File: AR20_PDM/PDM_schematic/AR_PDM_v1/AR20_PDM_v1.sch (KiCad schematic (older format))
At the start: 9 parts, among them J1 High_Curret_terminal, J2 ACM_Connector

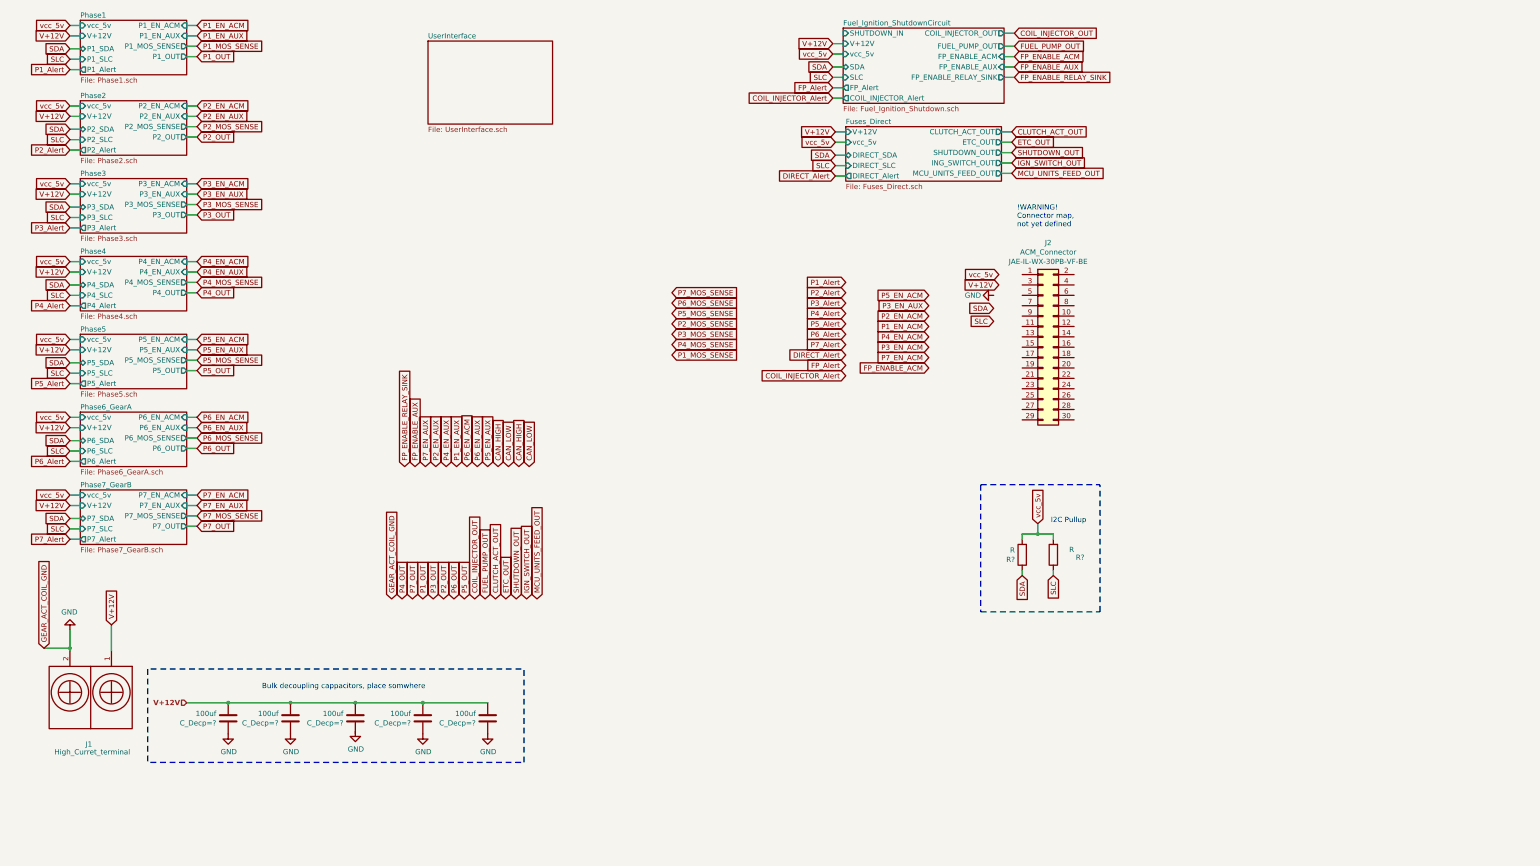
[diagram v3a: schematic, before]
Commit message: Added LEDs and switches.
- Added all status leds
- Added all switches
- ! Connections are work in progress, not everything is correct
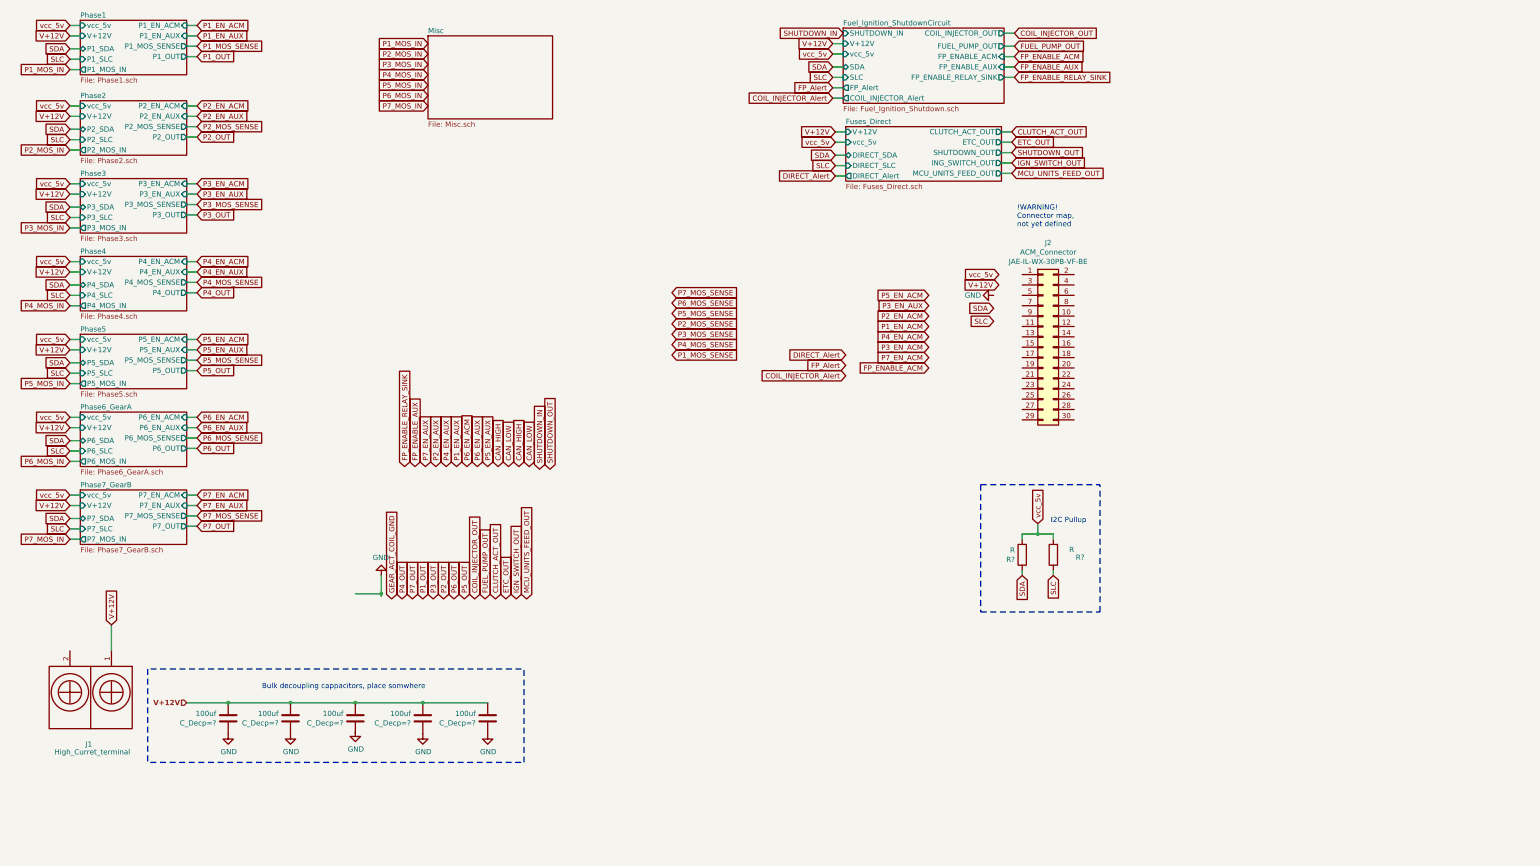
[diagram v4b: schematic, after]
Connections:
- net GND: no longer J1.2 (Pin_2)
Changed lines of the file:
@@
 F3 "P1_SDA" B L 1100 900 50
 F4 "P1_SLC" I L 1100 1000 50
-F5 "P1_Alert" O L 1100 1100 50
-F6 "V+12V" I L 1100 775 50
-F7 "P1_EN_ACM" I R 2125 675 50
-F8 "P1_EN_AUX" I R 2125 775 50
-F9 "P1_OUT" O R 2125 975 50
-F10 "P1_MOS_SENSE" O R 2125 875 50
+F5 "V+12V" I L 1100 775 50
+F6 "P1_EN_ACM" I R 2125 675 50
+F7 "P1_EN_AUX" I R 2125 775 50
+F8 "P1_OUT" O R 2125 975 50
+F9 "P1_MOS_SENSE" O R 2125 875 50
+F10 "P1_MOS_IN" O L 1100 1100 50
 $EndSheet
 Text GLabel 2225 875  2    50   Input ~ 0
@@
 	1000 1100 1100 1100
 Text GLabel 1000 1100 0    50   Input ~ 0
-P1_Alert
+P1_MOS_IN
 Wire Wire Line
 	1000 775  1100 775
@@
 	1000 1875 1100 1875
 Text GLabel 1000 1875 0    50   Input ~ 0
-P2_Alert
+P2_MOS_IN
 Wire Wire Line
 	1000 1550 1100 1550
@@
 F2 "vcc_5v" I L 1100 2200 50
 F3 "V+12V" I L 1100 2300 50
-F4 "P3_Alert" O L 1100 2625 50
-F5 "P3_SDA" B L 1100 2425 50
-F6 "P3_SLC" I L 1100 2525 50
-F7 "P3_EN_ACM" I R 2125 2200 50
-F8 "P3_EN_AUX" I R 2125 2300 50
-F9 "P3_MOS_SENSE" O R 2125 2400 50
-F10 "P3_OUT" O R 2125 2500 50
+F4 "P3_SDA" B L 1100 2425 50
+F5 "P3_SLC" I L 1100 2525 50
+F6 "P3_EN_ACM" I R 2125 2200 50
+F7 "P3_EN_AUX" I R 2125 2300 50
+F8 "P3_MOS_SENSE" O R 2125 2400 50
+F9 "P3_OUT" O R 2125 2500 50
+F10 "P3_MOS_IN" O L 1100 2625 50
 $EndSheet
 Text GLabel 2225 2400 2    50   Input ~ 0
@@
 	1000 2625 1100 2625
 Text GLabel 1000 2625 0    50   Input ~ 0
-P3_Alert
+P3_MOS_IN
 Wire Wire Line
 	1000 2300 1100 2300
@@
 	1000 3375 1100 3375
 Text GLabel 1000 3375 0    50   Input ~ 0
-P4_Alert
+P4_MOS_IN
 Wire Wire Line
 	1000 3050 1100 3050
@@
 F2 "vcc_5v" I L 1100 3700 50
 F3 "V+12V" I L 1100 3800 50
-F4 "P5_Alert" O L 1100 4125 50
-F5 "P5_SDA" B L 1100 3925 50
-F6 "P5_SLC" I L 1100 4025 50
-F7 "P5_EN_ACM" I R 2125 3700 50
-F8 "P5_EN_AUX" I R 2125 3800 50
-F9 "P5_MOS_SENSE" O R 2125 3900 50
-F10 "P5_OUT" O R 2125 4000 50
+F4 "P5_SDA" B L 1100 3925 50
+F5 "P5_SLC" I L 1100 4025 50
+F6 "P5_EN_ACM" I R 2125 3700 50
+F7 "P5_EN_AUX" I R 2125 3800 50
+F8 "P5_MOS_SENSE" O R 2125 3900 50
+F9 "P5_OUT" O R 2125 4000 50
+F10 "P5_MOS_IN" O L 1100 4125 50
 $EndSheet
 Text GLabel 2225 3900 2    50   Input ~ 0
@@
 	1000 4125 1100 4125
 Text GLabel 1000 4125 0    50   Input ~ 0
-P5_Alert
+P5_MOS_IN
 Wire Wire Line
 	1000 3800 1100 3800
@@
 F2 "vcc_5v" I L 1100 4450 50
 F3 "V+12V" I L 1100 4550 50
-F4 "P6_Alert" O L 1100 4875 50
-F5 "P6_SDA" B L 1100 4675 50
-F6 "P6_SLC" I L 1100 4775 50
-F7 "P6_EN_ACM" I R 2125 4450 50
-F8 "P6_EN_AUX" I R 2125 4550 50
-F9 "P6_MOS_SENSE" O R 2125 4650 50
-F10 "P6_OUT" O R 2125 4750 50
+F4 "P6_SDA" B L 1100 4675 50
+F5 "P6_SLC" I L 1100 4775 50
+F6 "P6_EN_ACM" I R 2125 4450 50
+F7 "P6_EN_AUX" I R 2125 4550 50
+F8 "P6_MOS_SENSE" O R 2125 4650 50
+F9 "P6_OUT" O R 2125 4750 50
+F10 "P6_MOS_IN" O L 1100 4875 50
 $EndSheet
 Text GLabel 2225 4650 2    50   Input ~ 0
@@
 	1000 4875 1100 4875
 Text GLabel 1000 4875 0    50   Input ~ 0
-P6_Alert
+P6_MOS_IN
 Wire Wire Line
 	1000 4550 1100 4550
@@
 	1400 6700 1400 6450
 Wire Wire Line
-	1000 6700 1000 6675
+	4000 6175 4000 6150
 $Comp
 L AR20_PDM_v1-rescue:GND-power #PWR?
 U 1 1 5E117EF0
-P 1000 6500
+P 4000 5975
 AR Path="/5DA89415/5E117EF0" Ref="#PWR?"  Part="1"
 AR Path="/5DA8920B/5E117EF0" Ref="#PWR?"  Part="1"
 AR Path="/5DE4D361/5E117EF0" Ref="#PWR?"  Part="1"
 AR Path="/5E117EF0" Ref="#PWR?"  Part="1"
-F 0 "#PWR?" H 1000 6250 50  0001 C CNN
-F 1 "GND" H 1005 6327 50  0000 C CNN
-F 2 "" H 1000 6500 50  0001 C CNN
-F 3 "" H 1000 6500 50  0001 C CNN
-	1    1000 6500
+F 0 "#PWR?" H 4000 5725 50  0001 C CNN
+F 1 "GND" H 4005 5802 50  0000 C CNN
+F 2 "" H 4000 5975 50  0001 C CNN
+F 3 "" H 4000 5975 50  0001 C CNN
+	1    4000 5975
 	-1   0    0    1
 $EndComp
@@
 	1000 5625 1100 5625
 Text GLabel 1000 5625 0    50   Input ~ 0
-P7_Alert
+P7_MOS_IN
 Wire Wire Line
 	1000 5300 1100 5300
@@
 F2 "vcc_5v" I L 1100 1450 50
 F3 "V+12V" I L 1100 1550 50
-F4 "P2_Alert" O L 1100 1875 50
-F5 "P2_SDA" B L 1100 1675 50
-F6 "P2_SLC" I L 1100 1775 50
-F7 "P2_EN_ACM" I R 2125 1450 50
-F8 "P2_EN_AUX" I R 2125 1550 50
-F9 "P2_MOS_SENSE" O R 2125 1650 50
-F10 "P2_OUT" O R 2125 1750 50
+F4 "P2_SDA" B L 1100 1675 50
+F5 "P2_SLC" I L 1100 1775 50
+F6 "P2_EN_ACM" I R 2125 1450 50
+F7 "P2_EN_AUX" I R 2125 1550 50
+F8 "P2_MOS_SENSE" O R 2125 1650 50
+F9 "P2_OUT" O R 2125 1750 50
+F10 "P2_MOS_IN" O L 1100 1875 50
 $EndSheet
 $Sheet
@@
 F2 "vcc_5v" I L 1100 2950 50
 F3 "V+12V" I L 1100 3050 50
-F4 "P4_Alert" O L 1100 3375 50
-F5 "P4_SDA" B L 1100 3175 50
-F6 "P4_SLC" I L 1100 3275 50
-F7 "P4_EN_ACM" I R 2125 2950 50
-F8 "P4_EN_AUX" I R 2125 3050 50
-F9 "P4_MOS_SENSE" O R 2125 3150 50
-F10 "P4_OUT" O R 2125 3250 50
+F4 "P4_SDA" B L 1100 3175 50
+F5 "P4_SLC" I L 1100 3275 50
+F6 "P4_EN_ACM" I R 2125 2950 50
+F7 "P4_EN_AUX" I R 2125 3050 50
+F8 "P4_MOS_SENSE" O R 2125 3150 50
+F9 "P4_OUT" O R 2125 3250 50
+F10 "P4_MOS_IN" O L 1100 3375 50
 $EndSheet
 $Sheet
@@
 F2 "vcc_5v" I L 1100 5200 50
 F3 "V+12V" I L 1100 5300 50
-F4 "P7_Alert" O L 1100 5625 50
-F5 "P7_SDA" B L 1100 5425 50
-F6 "P7_SLC" I L 1100 5525 50
-F7 "P7_EN_ACM" I R 2125 5200 50
-F8 "P7_EN_AUX" I R 2125 5300 50
-F9 "P7_MOS_SENSE" O R 2125 5400 50
-F10 "P7_OUT" O R 2125 5500 50
+F4 "P7_SDA" B L 1100 5425 50
+F5 "P7_SLC" I L 1100 5525 50
+F6 "P7_EN_ACM" I R 2125 5200 50
+F7 "P7_EN_AUX" I R 2125 5300 50
+F8 "P7_MOS_SENSE" O R 2125 5400 50
+F9 "P7_OUT" O R 2125 5500 50
+F10 "P7_MOS_IN" O L 1100 5625 50
 $EndSheet
 Wire Wire Line
@@
 Text GLabel 5200 6200 1    50   Input ~ 0
 ETC_OUT
+Text GLabel 5625 4950 1    50   Input ~ 0
+SHUTDOWN_OUT
 Text GLabel 5300 6200 1    50   Input ~ 0
-SHUTDOWN_OUT
+IGN_SWITCH_OUT
 Text GLabel 5400 6200 1    50   Input ~ 0
-IGN_SWITCH_OUT
-Text GLabel 5500 6200 1    50   Input ~ 0
 MCU_UNITS_FEED_OUT
-Text GLabel 750  6675 1    50   Input ~ 0
-GEAR_ACT_COIL_GND
-Wire Wire Line
-	750  6675 1000 6675
-Connection ~ 1000 6675
-Wire Wire Line
-	1000 6675 1000 6500
+Wire Wire Line
+	3750 6150 4000 6150
+Connection ~ 4000 6150
+Wire Wire Line
+	4000 6150 4000 5975
 Text GLabel 4100 6200 1    50   Input ~ 0
 GEAR_ACT_COIL_GND
@@
 Text GLabel 8475 4050 0    50   Input ~ 0
 COIL_INJECTOR_Alert
-Text GLabel 8475 3750 0    50   Input ~ 0
-P7_Alert
-Text GLabel 8475 3650 0    50   Input ~ 0
-P6_Alert
-Text GLabel 8475 3550 0    50   Input ~ 0
-P5_Alert
-Text GLabel 8475 3450 0    50   Input ~ 0
-P4_Alert
-Text GLabel 8475 3350 0    50   Input ~ 0
-P3_Alert
-Text GLabel 8475 3250 0    50   Input ~ 0
-P2_Alert
-Text GLabel 8475 3150 0    50   Input ~ 0
-P1_Alert
 Text GLabel 4225 4925 1    50   Input ~ 0
 FP_ENABLE_RELAY_SINK
@@
 CAN_LOW
 $Sheet
-S 4450 825  1200 800
+S 4450 775  1200 800
 U 5E5484EE
-F0 "UserInterface" 50
-F1 "UserInterface.sch" 50
+F0 "Misc" 50
+F1 "Misc.sch" 50
 $EndSheet
+Text GLabel 4450 850  0    50   Input ~ 0
+P1_MOS_IN
+Text GLabel 4450 950  0    50   Input ~ 0
+P2_MOS_IN
+Text GLabel 4450 1050 0    50   Input ~ 0
+P3_MOS_IN
+Text GLabel 4450 1150 0    50   Input ~ 0
+P4_MOS_IN
+Text GLabel 4450 1250 0    50   Input ~ 0
+P5_MOS_IN
+Text GLabel 4450 1350 0    50   Input ~ 0
+P6_MOS_IN
+Text GLabel 4450 1450 0    50   Input ~ 0
+P7_MOS_IN
+Text GLabel 8450 750  0    50   Input ~ 0
+SHUTDOWN_IN
+Text GLabel 5525 4950 1    50   Input ~ 0
+SHUTDOWN_IN
 $EndSCHEMATC

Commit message: Fixed wrong value components and ports, wiring, see discription
- Fixed supply cappacitor value 220 nf to 100nf
- Fixed IN cappacitor value 220 nf to 150 nf
- Fixed out cappacitor value, 220nf to 10 nf
- Made a mux for mosfet sense
- Found a I/O port expander
- Added some and removed some leds
- Fixed all labels, and wired everything up, besides the connectors
- Still missing connector and acm connector pinout.
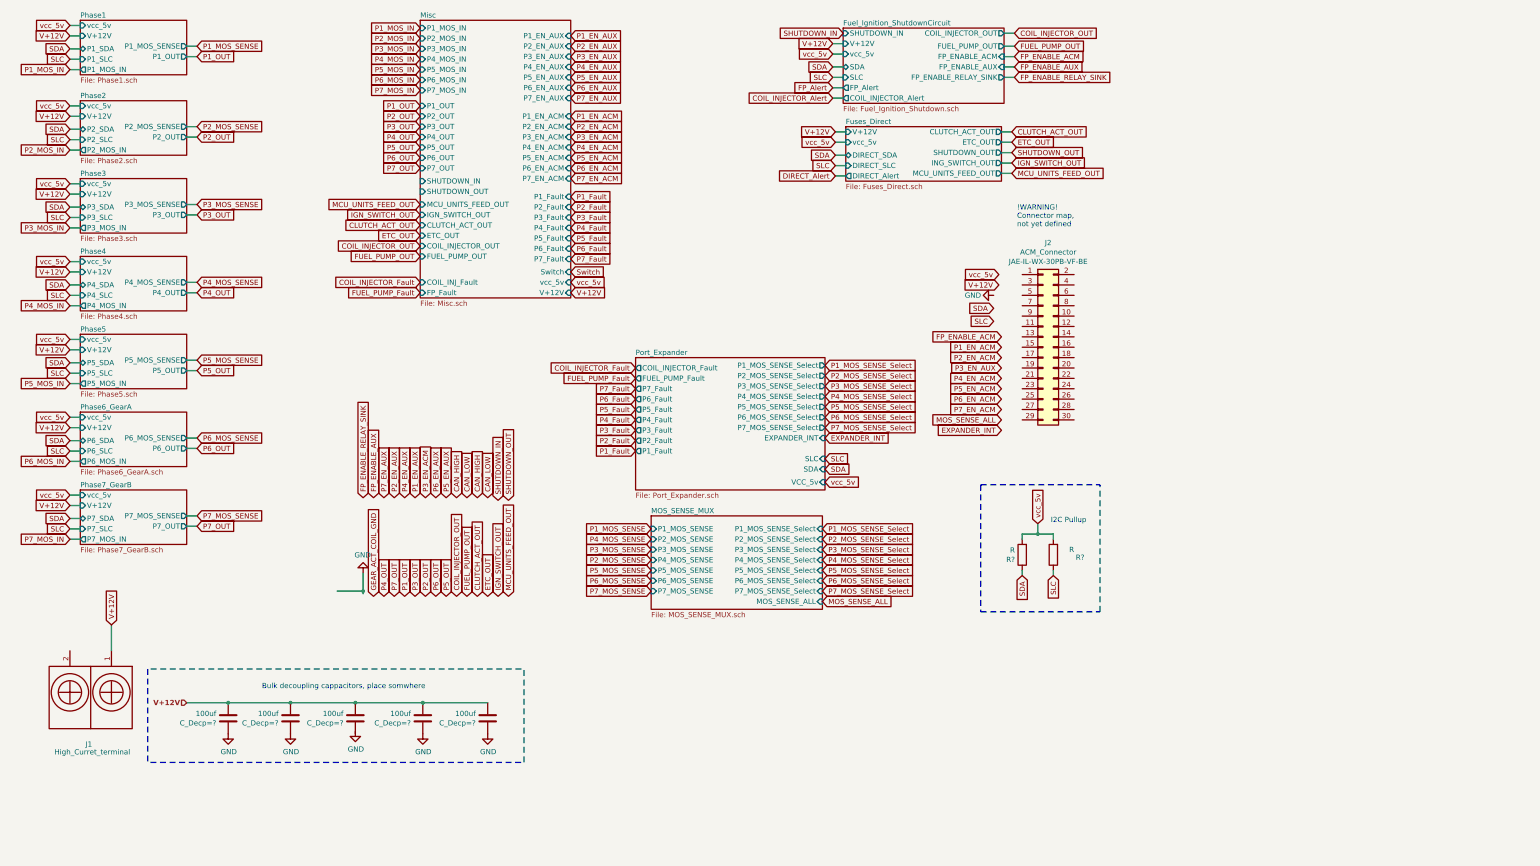
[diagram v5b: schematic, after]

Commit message: Fixed issues, controlled components, BOM, see discription
- added acm symbol
- fixed wrongly faced P-mosfets
- I/O expander now sinks led instead of source
- Bill of material mostly done
- Correct address for INA233 chips.
- Now 4 diodes serves as flyback for all mosfets
- Corrected naming scheme for compmonents (everything is not fixed yet)
- Fixed some labels
- altso some minor changes
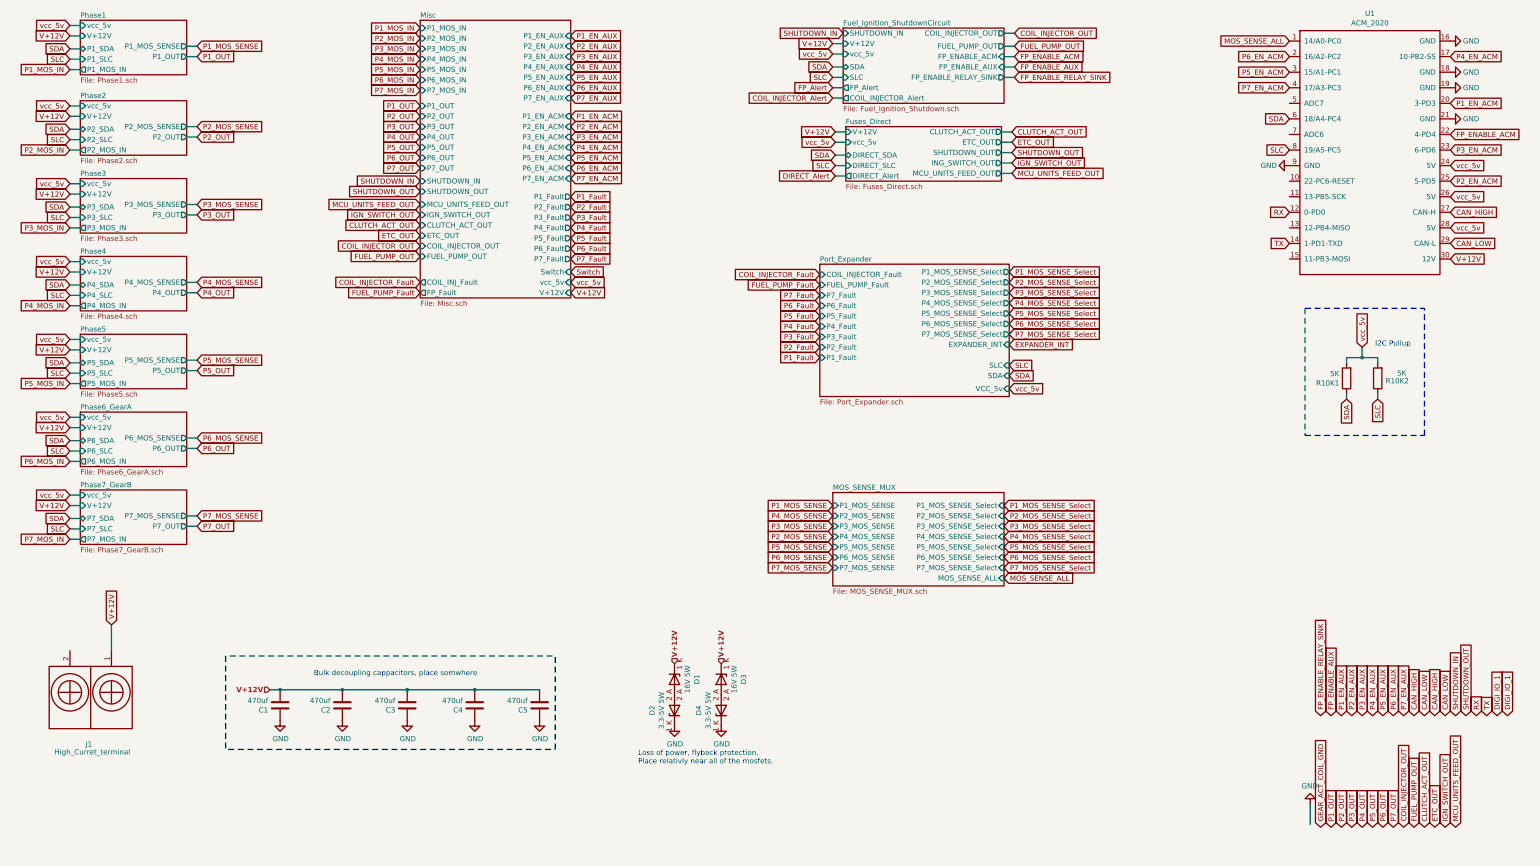
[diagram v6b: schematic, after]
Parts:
- removed J2: ACM_Connector, symbol Connector_Generic:Conn_02x15_Odd_Even
- removed R10K?: R, symbol AR20_PDM_v1-rescue:R-Device
- added D1, D3: 16V 5W, Diode_THT:D_5W_P10.16mm_Horizontal, symbol AR20_PDM_v1-rescue:D_Zener-Device
- added D2, D4: 3.3-5V 5W, Diode_THT:D_5W_P10.16mm_Horizontal, symbol AR20_PDM_v1-rescue:D_Zener-Device
- added R10K2: 5K, symbol AR20_PDM_v1-rescue:R-Device
- added U1: ACM_2020, symbol ACM_2020_Symbol:ACM_2020
- C1, C2, C3, C4, C5: renamed from C_Decp=?; value 100uf -> 470uf
- R10K1: renamed from R10K?; value R -> 5K
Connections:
- net CAN_HIGH: now also U1.27 (CAN-H)
- net CAN_LOW: now also U1.29 (CAN-L)
- net FP_ENABLE_ACM: now also U1.22 (4-PD4)
- net GND: now also C3.1, D2.1 (K), D4.1 (K), U1.16 (GND), U1.18 (GND), U1.19 (GND), U1.21 (GND), U1.9 (GND)
- net MOS_SENSE_ALL: now also U1.1 (14/A0-PC0)
- net P1_EN_ACM: now also U1.20 (3-PD3)
- net P2_EN_ACM: now also U1.25 (5-PD5)
- net P3_EN_ACM: now also U1.23 (6-PD6)
- net P4_EN_ACM: now also U1.17 (10-PB2-SS)
- net P5_EN_ACM: now also U1.3 (15/A1-PC1)
- net P6_EN_ACM: now also U1.2 (16/A2-PC2)
- net P7_EN_ACM: now also U1.4 (17/A3-PC3)
- net SDA: now also U1.6 (18/A4-PC4)
- net SLC: now also R10K2.1, U1.8 (19/A5-PC5)
- net V+12V: now also D1.1 (K), D3.1 (K), U1.30 (12V)
- net vcc_5v: now also R10K2.2, U1.24 (5V), U1.26 (5V), U1.28 (5V)
- new net: D1.2 (A), D2.2 (A)
- new net: D3.2 (A), D4.2 (A)
- new net RX: U1.12 (0-PD0)
- new net TX: U1.14 (1-PD1-TXD)
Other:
- note added: "Loss of power, flyback protection. \nPlace relativly near all of the mosfets."
- note removed: "!WARNING!\nConnector map,\nnot yet defined"
- moved on the sheet: C1, C2, C3, C4, C5, R10K1

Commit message: PCB design, and issue fixing, work in progress
- Error fixed: Mux mosfet resistor change to ground
- Open drain output added on phase 6, for engine blipping purpose
- Most of pcb symbols and footprints are finished, including main connector
- PCB is change from 1oz to 2oz copper layer, for easier routing.
- Basic Draft of pcb is done, for now.
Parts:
- added J2: 1-776163-1, AR_PDM_v1:TE_1-776163-1, symbol AR20_PDM_v1-rescue:1-776163-1
- C1, C2, C3, C4, C5: footprint (none) -> AR_PDM_v1:CAPAE1350X1400N_EEV-FK1V471Q; symbol AR20_PDM_v1-rescue:C-Device -> AR20_PDM_v1-rescue:CP1
- J1: footprint (none) -> Connector_Coaxial:SMA_Amphenol_132291_Vertical
- R10K1, R10K2: footprint (none) -> Resistor_SMD:R_0603_1608Metric
- U1: footprint (none) -> AR_PDM_v1:ACM_2020_Footprint
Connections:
- net GND: now also C1.2, C2.2, C3.2, C4.2, C5.2; no longer C1.1, C2.1, C3.1, C4.1, C5.1
- net V+12V: now also C1.1, C2.1, C3.1, C4.1, C5.1; no longer C1.2, C2.2, C3.2, C4.2, C5.2
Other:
- note added: "15 pinns"
- moved on the sheet: R10K1, R10K2
